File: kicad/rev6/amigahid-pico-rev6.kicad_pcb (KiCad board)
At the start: 2 copper layers, 100 x 80 mm, 115 parts, among them J1 A500 KBD OUT, J10 PS/2 KBD OUT, J11 DIN5 KBD IN, J12 PS/2 KBD IN, J13 USB-C AUX 5V, J2 DEBUG UART+SWD, J3 OLED I2C, J4 USB-A HOST, J7 SPARE GP28, J8 A500 KBD IN, J9 DIN5 KBD OUT, P1 DE9 MALE PORT 1, P2 DE9 MALE PORT 2, Q1 BSS138, Q10 BSS138, Q11 BSS138, Q12 BSS138, Q13 BSS138, Q14 BSS138, Q15 BSS138, Q16 BSS138, Q17 BSS138, Q18 BSS138, Q19 BSS138, Q2 BSS138, Q3 BSS138, Q4 BSS138, Q5 BSS138, Q6 BSS138, Q7 BSS138, Q8 BSS138, Q9 BSS138, U1 PicoW, U2 USBLC6-2SC6

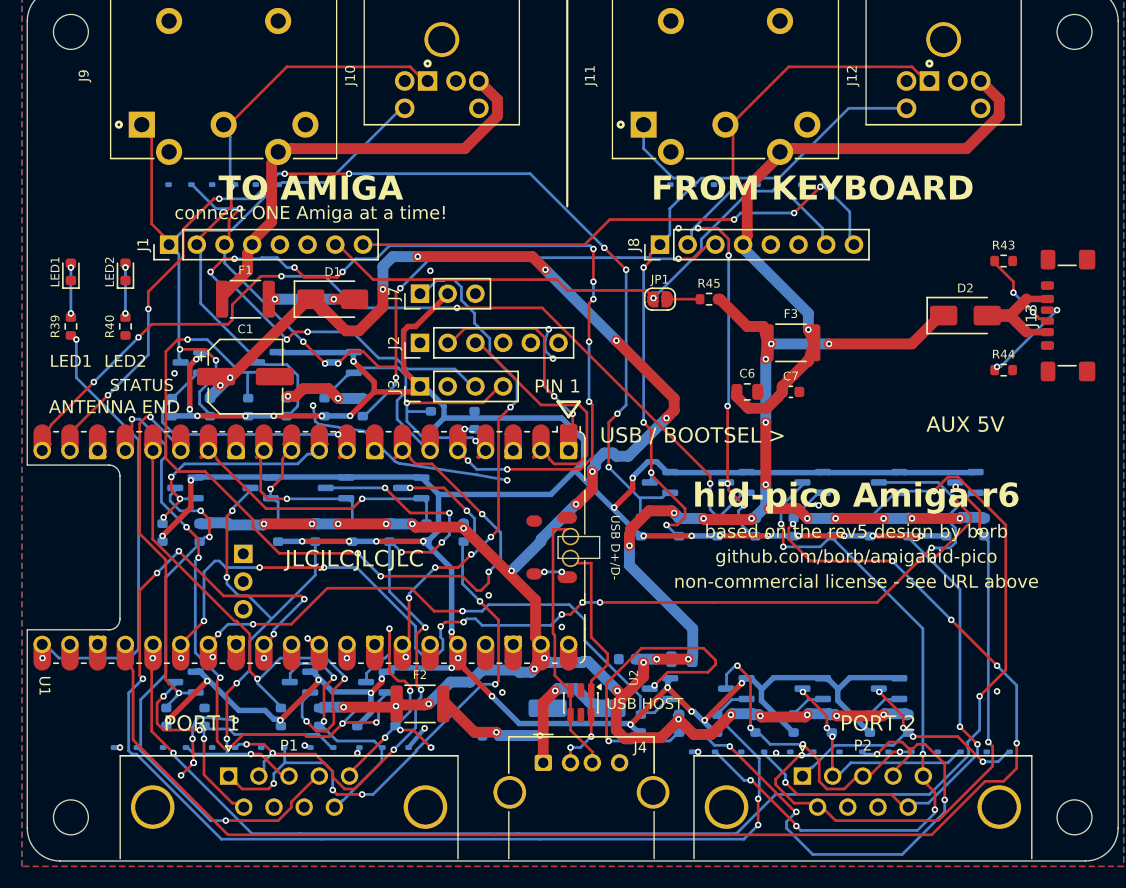
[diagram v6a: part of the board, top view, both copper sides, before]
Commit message: kicad: move the esd clamps to the pins they protect, and re-lay the copper
the clamp rows were laid out in designator order rather than connector-pin order, so
a clamp could sit 19.2 mm from the pin it protects with the stub running past the
level shifter it is meant to shield.  D22 was 19.22 mm from P2 pin 5, D28 19.12 mm
from P2 pin 1, D13 16.92 mm from P1 pin 4.  each row is now re-ordered to follow its
connector's pin order and pulled up against the connector, and the outer clamps are
mirrored so the signal pad always faces its pin.  worst stub 19.22 mm -> 7.05 mm.

U2's two I/O columns were mirrored with respect to J4, so the differential pair
crossed over between the filter and the socket and needed a via each to get past
itself.  turning the part 180 degrees lines both columns up, takes those two vias out
of the pair, and brings pin 5 (VBUS) alongside the rail that feeds it - it was
floating before, because a 1.0 mm power track cannot reach a pin whose neighbours are
0.95 mm away.  it now gets the pad neckdown the rules allow, 0.40 mm for 1.7 mm, and
a via down to the rail.

the USB pair is laid by hand: it is the only pair with a length budget, and the tap
slot is an edge to keep 0.35 mm away from rather than the 0.305/0.315 mm it had.
dp leaves the slot on the north side and goes round its east end, dm leaves on the
south side and drops through the gap between the module's pads 39 and 40; dm is
deliberately longer than it needs to be, because matching dp is worth more than 3 mm.
22.97 and 24.53 mm, 1.56 mm apart, no vias in either.

everything else is re-routed, because rt.obstacles() shipped with VIA_HOLE_FACTOR = 0
- a track was allowed to run right up against a via's drill.  that was a deliberate
cheat while the board carried 1021 stitching vias, and with them gone it came due as
106 hole-clearance errors across nearly every net.  the rule is on now.  SYS5V is laid
first (1.0 mm, 29 pads, it needs the wide lanes), then +3V3 (a forty-pad comb along
the sh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
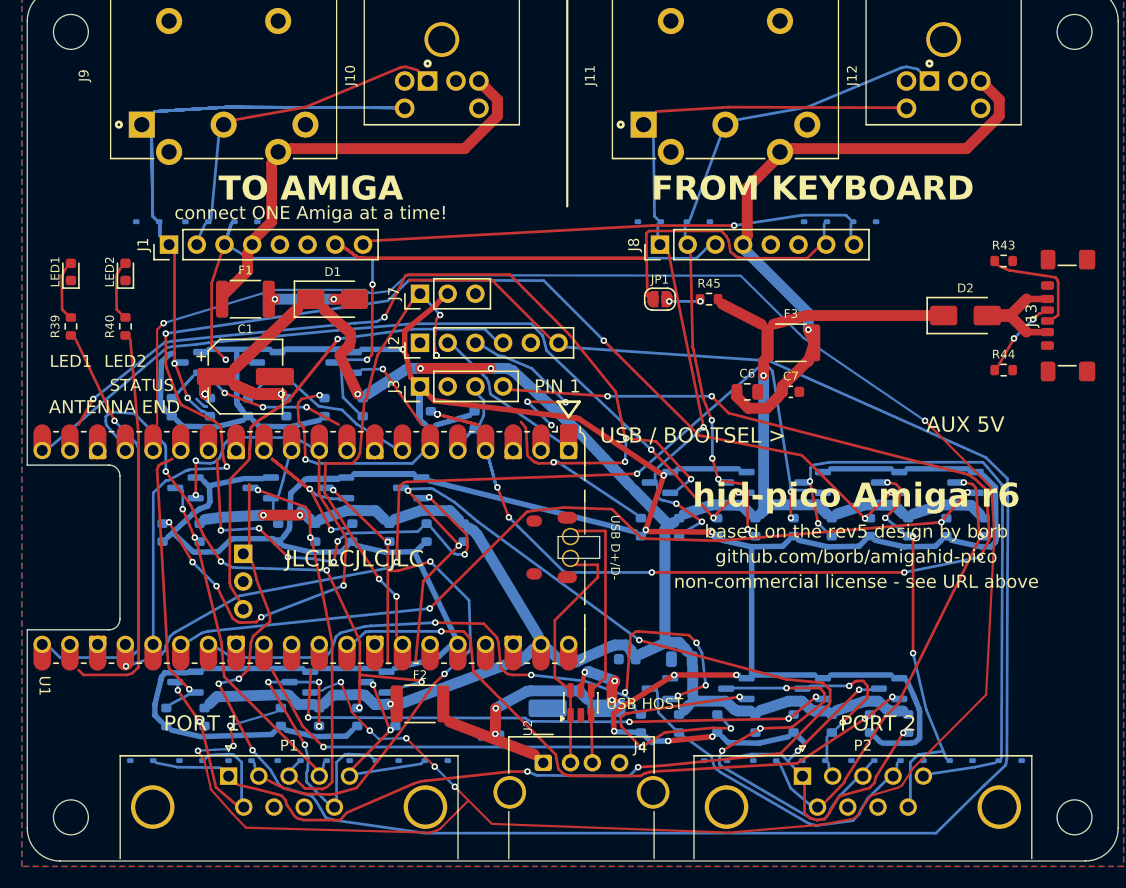
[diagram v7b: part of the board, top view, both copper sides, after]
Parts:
- moved D22 28.1 mm to (90.1, 70.8), turned to 0 degrees
- moved D28 25.9 mm to (63.1, 70.8)
- moved D13 19.5 mm to (28.5, 70.8), turned to 0 degrees
- moved D23 19.1 mm to (85.6, 70.8), turned to 0 degrees
- moved D27 12.4 mm to (72.1, 70.8)
- moved D16 12.1 mm to (10.5, 70.8)
- moved D17 12.1 mm to (15.0, 70.8)
- moved D12 11.5 mm to (11.0, 21.4)
- moved D14 10.6 mm to (24.0, 70.8)
- moved D10 6.93 mm to (20.0, 21.4), turned to 0 degrees
- moved D30 5.85 mm to (76.8, 21.4), turned to 0 degrees
- moved D25 5.66 mm to (81.1, 70.8), turned to 0 degrees
- moved D29 5.45 mm to (72.3, 21.4)
- moved D20 4.52 mm to (57.0, 21.4)
- moved D21 4.21 mm to (61.5, 21.4), turned to 0 degrees
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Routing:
- net /swclk: track 0.00 -> 185.5 mm, vias 0 -> 3
- net /cont1_b2_lo: track 51.3 -> 225.0 mm, vias 3 -> 10
- net /kb_pwrled: track 55.1 -> 220.3 mm, vias 1 -> 0
- net /kbclock: track 59.9 -> 198.7 mm
- net /i2c_sda: track 23.8 -> 123.6 mm, vias 2 -> 13
- net /i2c_scl: track 104.0 -> 6.44 mm, vias 14 -> 0
- net /cont1_v: track 59.3 -> 128.2 mm, vias 7 -> 5
- net /kbdata_lo: track 79.7 -> 14.5 mm, vias 5 -> 0
- net /cont2_vq_lo: track 118.4 -> 61.6 mm, vias 8 -> 4
- net /swdio: track 0.00 -> 56.8 mm, vias 0 -> 1
- net /cont2_v_lo: track 4.47 -> 58.8 mm, vias 1 -> 3
- net /cont2_hq: track 80.8 -> 27.6 mm, vias 6 -> 0
- net /cont2_b3_lo: track 135.1 -> 88.4 mm
- net /cont2_h_lo: track 6.05 -> 51.4 mm, vias 1 -> 4
- net GND: track 39.0 -> 0.00 mm, vias 25 -> 0
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
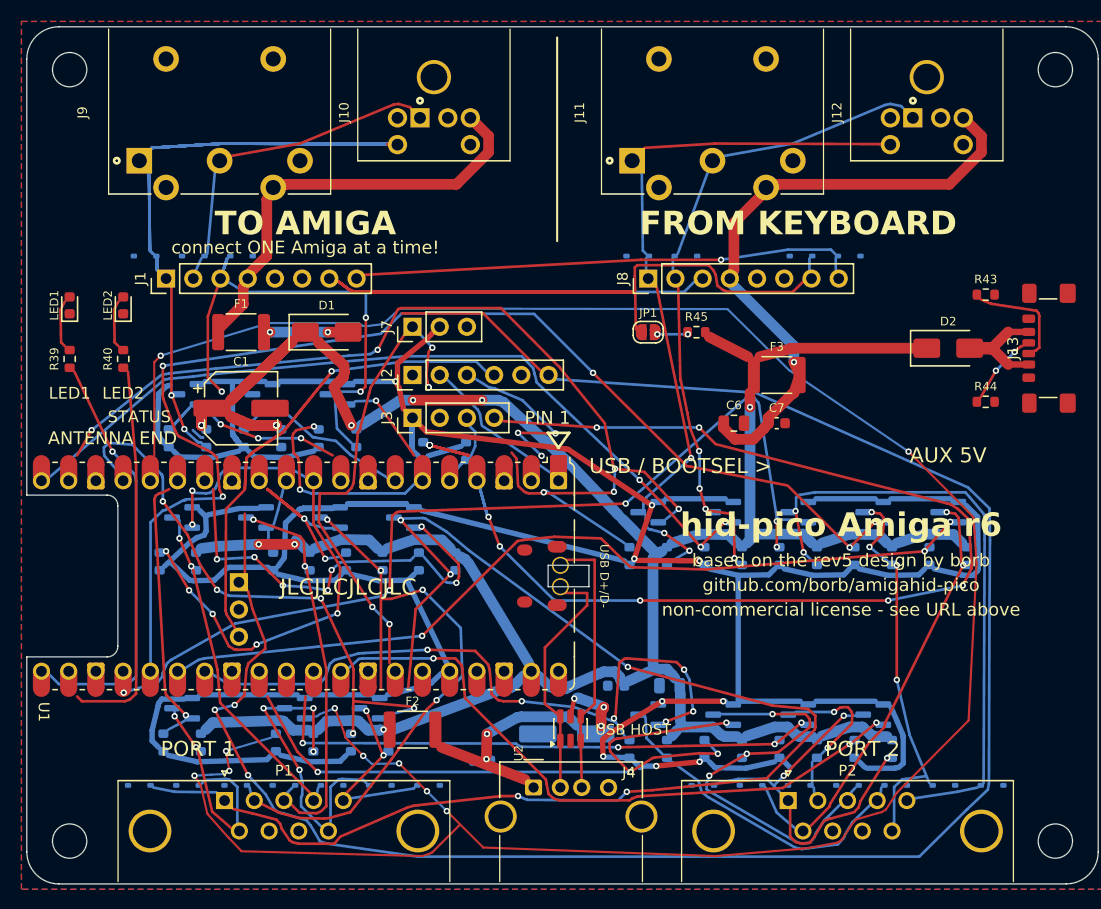
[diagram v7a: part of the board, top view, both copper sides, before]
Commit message: kicad: stitch the rev6 ground back in and finish the copper
ground last, on an 8 mm grid rather than the 2.5 mm one it started with: 18 clamps get
their own anchor via before anything else, then the grid, then the leftover pour
islands are tied in.  114 vias where there were 1021, and every via is now placed with
the signals already down instead of the other way round.

the module's ground pads, J2's, J4's and P1's shell came up as starved thermals - the
pour can only reach them from one side, so DRC called the relief incomplete.  they are
ground pads on a ground plane and the module is reflowed by its castellations or
socketed, so they get a solid zone connection rather than two 0.5 mm spokes.

rt.pad_stamp models any pad that is not a circle or an oval as a plain rectangle, so
on the module's castellation pads - 1.6 x 3.2 mm roundrects with a 0.5 corner ratio,
i.e. stadiums - the router was ending routes in corners the real pad does not occupy.
the model said connected, KiCad said not.  those ends are carried through to the pad
centre, which closed thirteen nets that were reported open.

what is left, honestly:

  /kbdata will not close.  Q2's source pad and R4's pull-up sit on opposite corners of
  a 5 mm pocket with /kbdata_lo across the diagonal between them - the two nets have
  to cross, and SYS5V owns the front copper there.  clearing the whole pocket lets
  /kbdata through but always costs two or three of its neighbours their route.  the
  real fix is placement, not routing: every divider pair is mirrored with respect to
  the FET it serves (the 3V3-side pull-up sits over the drain pad and the 5V-side one
  over the source pad, when each wants the other), so all nineteen shifters route
  across themselves.  swapping the two resistors in each pair would remove nineteen
  crossings at once.

  D13's and D15's ground pads are still on pour islands of their own; the port-1 stub
  routing pinches the pour off around them and no lane can be freed for a tie withou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
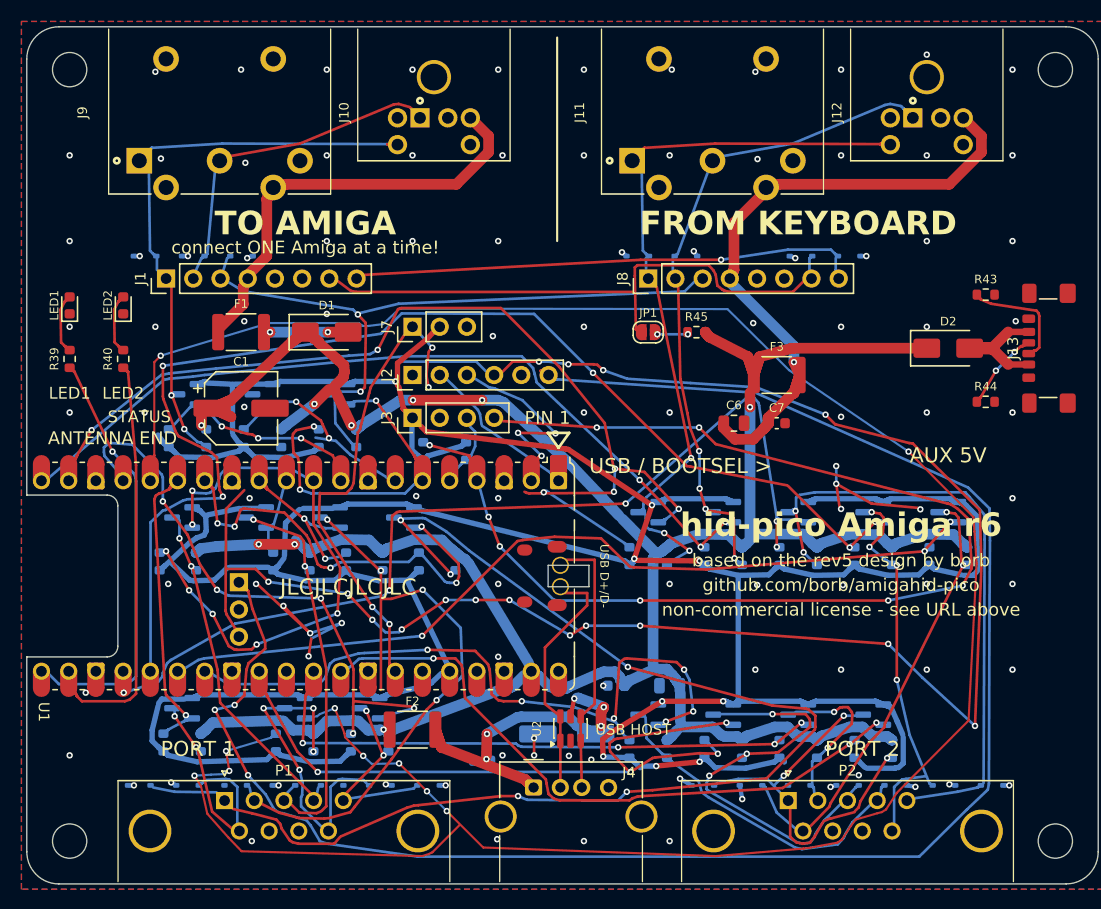
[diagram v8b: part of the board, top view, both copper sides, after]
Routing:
- net /kb_pwrled: track 220.3 -> 55.2 mm
- net /kbclock: track 198.7 -> 59.3 mm
- net /swdio: track 56.8 -> 170.7 mm, vias 1 -> 16
- net +3V3: track 356.1 -> 431.6 mm
- net GND: track 0.00 -> 43.2 mm, vias 0 -> 103
- net /SYS5V: track 275.2 -> 315.3 mm, vias 20 -> 9
- net /cont1_b1_lo: track 24.4 -> 48.0 mm
- net /kbreset: track 80.7 -> 61.2 mm, vias 3 -> 2
- net /kbin_clk: track 61.5 -> 78.5 mm
- net /gp28: track 41.8 -> 57.8 mm, vias 5 -> 4
- net /USBA_5V: track 25.7 -> 40.0 mm
- net /swclk: track 185.5 -> 172.5 mm
- net /cont1_v: track 128.2 -> 116.3 mm
- net /kbreset_lo: track 26.8 -> 38.4 mm
- net /KBIN_5V: track 58.1 -> 69.2 mm
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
